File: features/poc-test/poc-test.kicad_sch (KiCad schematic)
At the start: 5 parts, among them Q1 BC846BLP4, Q2 BC846BLP4

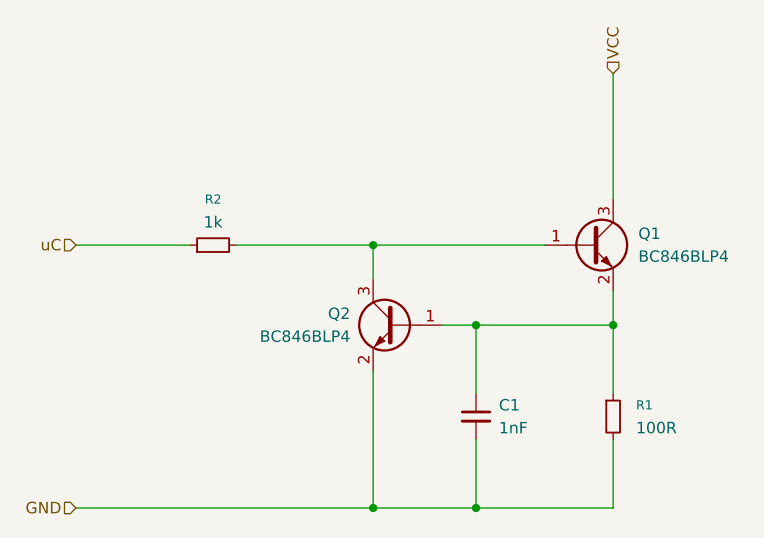
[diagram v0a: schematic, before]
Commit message: test(poc-test): change R1 100R→220R, R2 1k→2k2, bump rev to 2
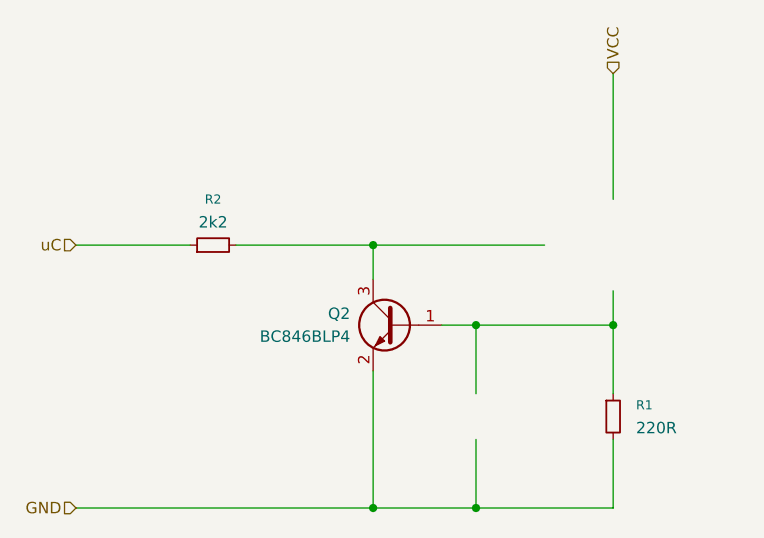
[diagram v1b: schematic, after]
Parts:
- removed C1: 1nF, Capacitor_SMD:C_0603_1608Metric, symbol Device:C_Small
- removed Q1: BC846BLP4, Package_DFN_QFN:Diodes_DFN1006-3, symbol Transistor_BJT:BC846BLP4
- R1: value 100R -> 220R
- R2: value 1k -> 2k2
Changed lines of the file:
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@@
 	(title_block
 		(title "Test Current Sink")
-		(date "2026-04-30")
-		(rev "1")
+		(date "2026-05-01")
+		(rev "2")
 		(company "Test Company")
 	)
@@
 			)
 		)
-		(property "Value" "100R"
+		(property "Value" "220R"
 			(at 125.73 76.1999 0)
 			(show_name no)
@@
 			)
 		)
-		(property "Value" "1k"
+		(property "Value" "2k2"
 			(at 78.74 53.34 90)
 			(show_name no)
@@
 			)
 		)
-		(pin "1"
-		)
-		(pin "2"
-		)
-		(pin "3"
+		(property "ki_keywords" "NPN Transistor"
+			(at 99.06 64.77 0)
+			(hide yes)
+			(show_name no)
+			(do_not_autoplace no)
+			(effects
+				(font
+					(size 1.27 1.27)
+				)
+			)
+		)
+		(property "ki_fp_filters" "Diodes*DFN1006*"
+			(at 99.06 64.77 0)
+			(hide yes)
+			(show_name no)
+			(do_not_autoplace no)
+			(effects
+				(font
+					(size 1.27 1.27)
+				)
+			)
 		)
 		(instances
@@
 		)
 	)
-	(symbol
-		(lib_id "Device:C_Small")
-		(at 107.95 74.93 0)
-		(unit 1)
-		(body_style 1)
-		(exclude_from_sim no)
-		(in_bom yes)
-		(on_board yes)
-		(in_pos_files yes)
-		(dnp no)
-		(fields_autoplaced yes)
-		(property "Reference" "C1"
-			(at 110.49 73.6662 0)
-			(show_name no)
-			(do_not_autoplace no)
-			(effects
-				(font
-					(size 1.27 1.27)
-				)
-				(justify left)
-			)
-		)
-		(property "Value" "1nF"
-			(at 110.49 76.2062 0)
-			(show_name no)
-			(do_not_autoplace no)
-			(effects
-				(font
-					(size 1.27 1.27)
-				)
-				(justify left)
-			)
-		)
-		(property "Footprint" "Capacitor_SMD:C_0603_1608Metric"
-			(at 107.95 74.93 0)
-			(hide yes)
-			(show_name no)
-			(do_not_autoplace no)
-			(effects
-				(font
-					(size 1.27 1.27)
-				)
-			)
-		)
-		(property "Datasheet" ""
-			(at 107.95 74.93 0)
-			(hide yes)
-			(show_name no)
-			(do_not_autoplace no)
-			(effects
-				(font
-					(size 1.27 1.27)
-				)
-			)
-		)
-		(property "Description" "Unpolarized capacitor, small symbol"
-			(at 107.95 74.93 0)
-			(hide yes)
-			(show_name no)
-			(do_not_autoplace no)
-			(effects
-				(font
-					(size 1.27 1.27)
-				)
-			)
-		)
-		(pin "1"
-		)
-		(pin "2"
-		)
-		(instances
-			(project "poc-test"
-				(path "/d56f88c0-57bc-445a-b022-9faabb5ff772"
-					(reference "C1")
-					(unit 1)
-				)
-			)
-		)
-	)
-	(symbol
-		(lib_id "Transistor_BJT:BC846BLP4")
-		(at 120.65 55.88 0)
-		(unit 1)
-		(body_style 1)
-		(exclude_from_sim no)
-		(in_bom yes)
-		(on_board yes)
-		(in_pos_files yes)
-		(dnp no)
-		(property "Reference" "Q1"
-			(at 125.984 54.61 0)
-			(show_name no)
-			(do_not_autoplace no)
-			(effects
-				(font
-					(size 1.27 1.27)
-				)
-				(justify left)
-			)
-		)
-		(property "Value" "BC846BLP4"
-			(at 125.984 57.15 0)
-			(show_name no)
-			(do_not_autoplace no)
-			(effects
-				(font
-					(size 1.27 1.27)
-				)
-				(justify left)
-			)
-		)
-		(property "Footprint" "Package_DFN_QFN:Diodes_DFN1006-3"
-			(at 125.73 57.785 0)
-			(hide yes)
-			(show_name no)
-			(do_not_autoplace no)
-			(effects
-				(font
-					(size 1.27 1.27)
-					(italic yes)
-				)
-				(justify left)
-			)
-		)
-		(property "Datasheet" "https://www.diodes.com/datasheet/download/BC846BLP4.pdf"
-			(at 120.65 55.88 0)
-			(hide yes)
-			(show_name no)
-			(do_not_autoplace no)
-			(effects
-				(font
-					(size 1.27 1.27)
-				)
-				(justify left)
-			)
-		)
-		(property "Description" "0.1A Ic, 65V Vce, NPN Transistor, DFN1006-3"
-			(at 120.65 55.88 0)
-			(hide yes)
-			(show_name no)
-			(do_not_autoplace no)
-			(effects
-				(font
-					(size 1.27 1.27)
-				)
-			)
-		)
-		(property "Sim.Device" "NPN"
-			(at 120.65 55.88 0)
-			(hide yes)
-			(show_name no)
-			(do_not_autoplace no)
-			(effects
-				(font
-					(size 1.27 1.27)
-				)
-			)
-		)
-		(property "Sim.Pins" "1=B 2=E 3=C"
-			(at 120.65 55.88 0)
-			(hide yes)
-			(show_name no)
-			(do_not_autoplace no)
-			(effects
-				(font
-					(size 1.27 1.27)
-				)
-			)
-		)
-		(pin "1"
-		)
-		(pin "2"
-		)
-		(pin "3"
-		)
-		(instances
-			(project "poc-test"
-				(path "/d56f88c0-57bc-445a-b022-9faabb5ff772"
-					(reference "Q1")
-					(unit 1)
-				)
-			)
-		)
-	)
-	(sheet_instances
-		(path "/"
-			(page "1")
-		)
-	)
-	(embedded_fonts no)
 )
